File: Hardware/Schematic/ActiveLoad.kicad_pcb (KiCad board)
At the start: 2 copper layers, 50 x 100 mm, 80 parts, among them P1 USB_OTG, P2 Banana jacks, P3 AKL 101-2, P4 TC2030-CTX, Q1 BTS117, SW1 FSMSM, SW2 ESP4020, U1 MAX3207E, U2 STM32F072C8, U3 DS18B20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

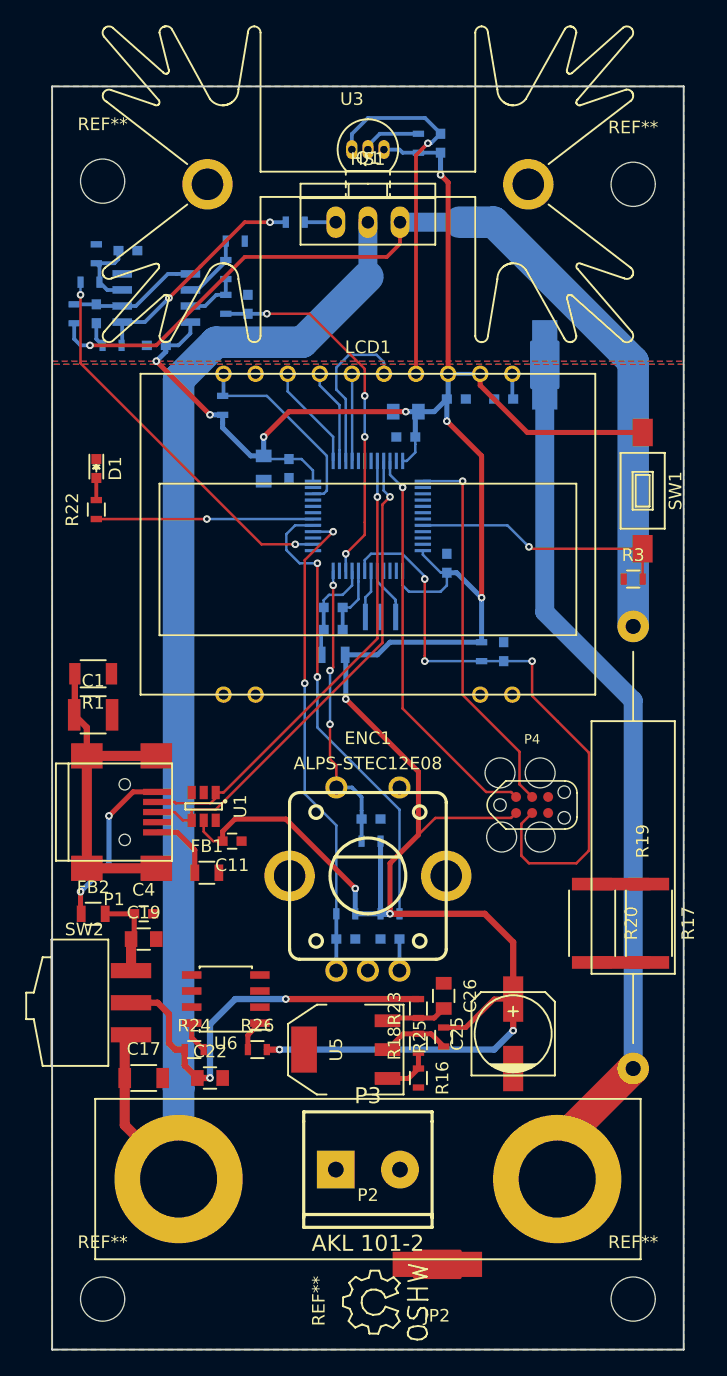
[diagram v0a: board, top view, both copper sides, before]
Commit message: updated schematic (TEMP pin and LED pin) finished PCB
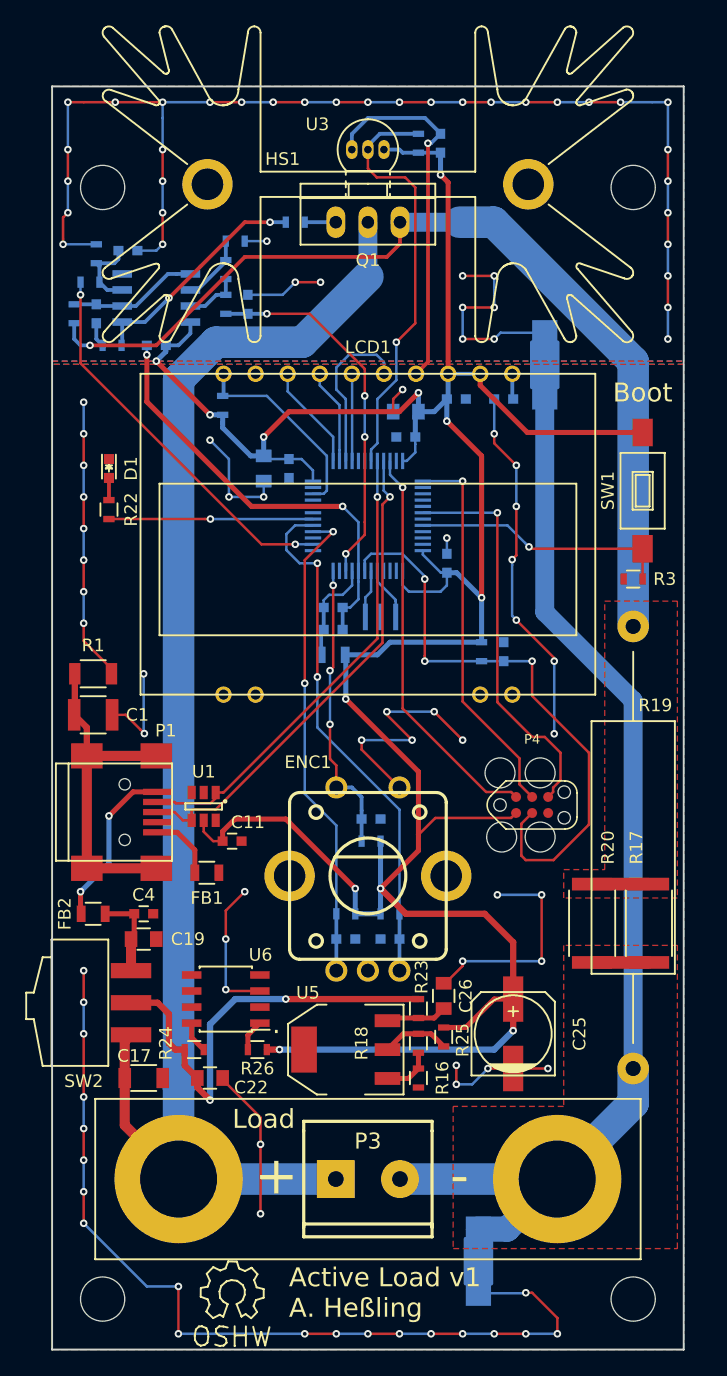
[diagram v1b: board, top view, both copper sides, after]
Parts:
- JP2: moved to B.Cu
- moved REF** 11.3 mm to (84.2, 128.0), turned to 0 degrees
- moved JP2 3.26 mm to (103.8, 125.5), turned to 270 degrees
- moved D1 1.00 mm to (74.5, 62.8)
- moved R22 1.00 mm to (74.5, 66.0)
- moved P3 0.75 mm to (95.0, 119.0)
- moved REF** 0.50 mm to (74.0, 40.5)
- moved REF** 0.25 mm to (116.0, 40.5)
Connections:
- P4 pad 6: (no net) -> UART1_TX
- U2 pad 31: (no net) -> TEMP
- U2 pad 42: (no net) -> UART1_TX
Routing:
- net GND: track 29.3 -> 239.2 mm, vias 1 -> 60
- net GNDA: track 5.52 -> 152.9 mm, vias 0 -> 44
- net UART1_TX: track 0.00 -> 31.5 mm, vias 0 -> 1
- net TEMP: track 4.69 -> 33.7 mm, vias 0 -> 1
- net GNDPWR: track 71.8 -> 92.1 mm
- net VCC: track 99.4 -> 111.8 mm
- net +3V3: track 234.2 -> 237.5 mm, vias 12 -> 13
- net Net-(C22-Pad1): track 32.4 -> 35.3 mm
- net ENC_B: track 39.5 -> 41.5 mm
- net NRST: track 48.4 -> 47.0 mm
- net Net-(R22-Pad1): track 17.2 -> 16.2 mm
- added copper zone on F.Cu, net GNDPWR
- added copper zone on F.Cu, net Net-(Q1-Pad3)
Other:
- rule trace_min: 0.15 -> 0.2
- board text added: "+"
- board text added: "-"
- board text added: "."
- board text added: "Active Load v1 A. Heßling"
- board text added: "Boot"
- board text added: "Load"

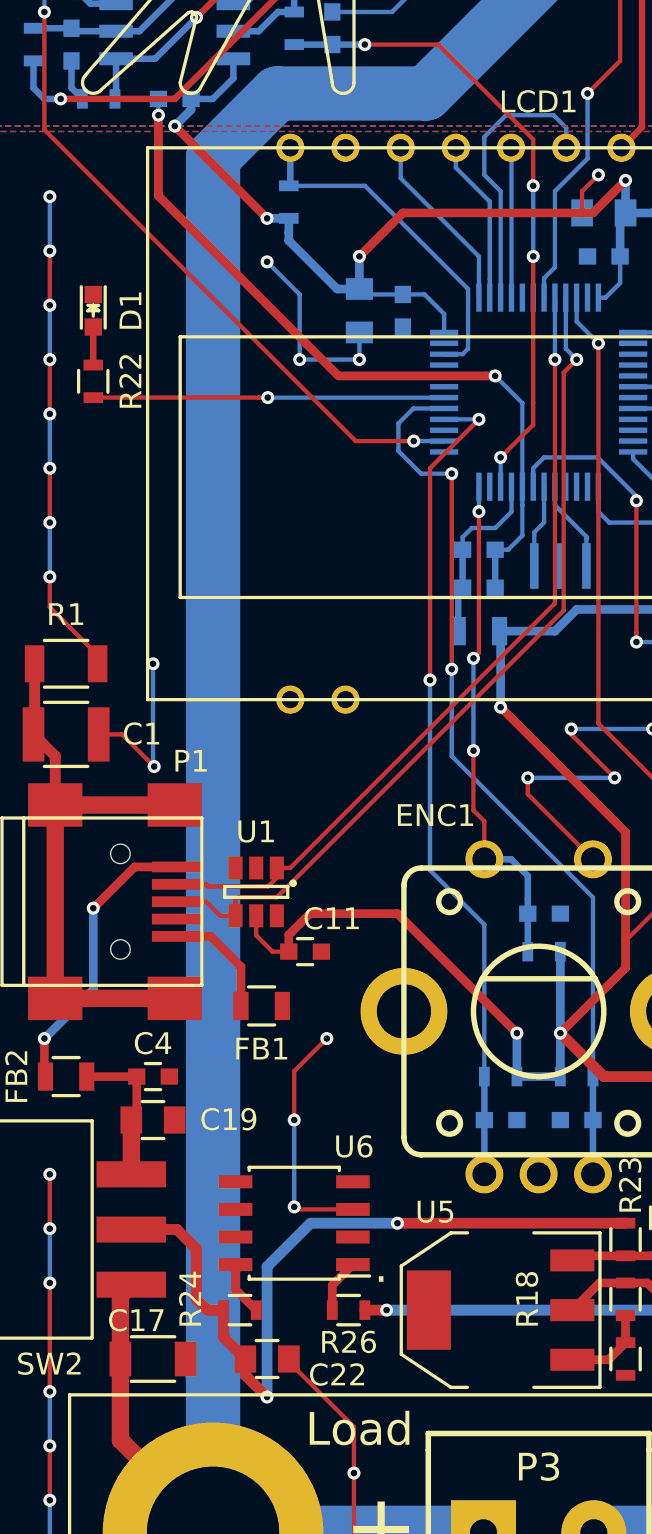
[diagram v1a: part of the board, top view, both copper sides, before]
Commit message: updated schematic and PCB (added VSENSE)
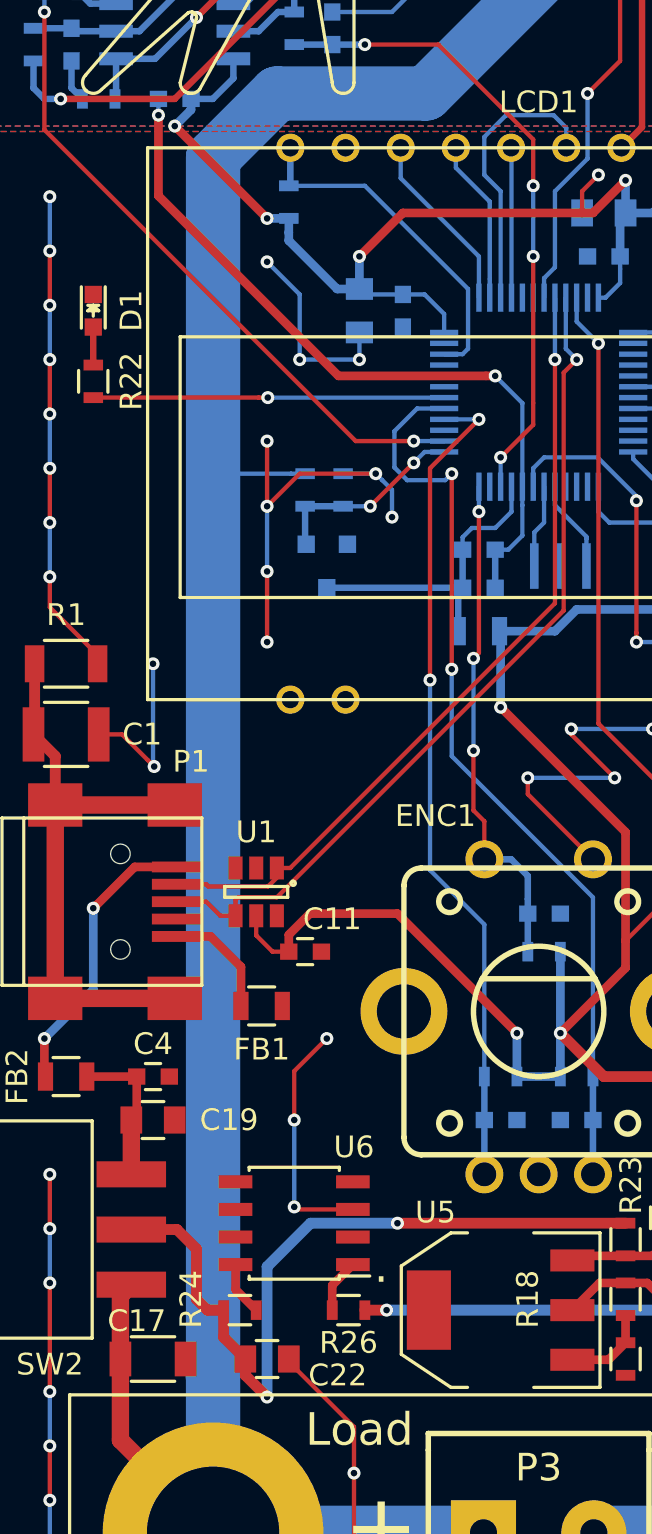
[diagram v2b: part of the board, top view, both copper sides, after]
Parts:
- added D2: BAS40, TO_SOT_Packages_SMD:SOT-23, B.Cu at (85.2, 74.5)
- added R27: 56k, Resistors_SMD:R_0603, B.Cu at (84.2, 71.0)
- added R28: 4k7, Resistors_SMD:R_0603, B.Cu at (86.0, 71.0)
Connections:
- U2 pad 13: (no net) -> VSENSE
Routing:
- net GND: track 239.2 -> 257.9 mm, vias 60 -> 66
- net VSENSE: track 0.00 -> 9.21 mm, vias 0 -> 2
- net +3.3VADC: track 8.29 -> 14.5 mm
- net VCC: track 111.8 -> 116.1 mm
- net ENC_B: track 41.5 -> 42.3 mm
